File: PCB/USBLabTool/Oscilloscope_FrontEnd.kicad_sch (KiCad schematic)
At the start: 92 parts, among them J10 T_pwm, J11 T_buf, J12 T_buf, J13 ADC2, J14 ADC1, J15 +3.3VA, J16 +3.3VA, J3 T_att, J4 T_att, J5 T_acdc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

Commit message: final version prototype
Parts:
- D1: footprint Diode_THT:D_DO-35_SOD27_P7.62mm_Horizontal -> Diode_SMD:D_SOD-323_HandSoldering
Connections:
- net GND: no longer C1.1, C4.2, C5.1, C8.2, R2.1, R3.1, R5.1, R8.1
- net GNDA: now also C1.1, C4.2, C5.1, C8.2, R2.1, R3.1, R5.1, R8.1

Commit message: change scope diode footprint
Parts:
- D2: footprint Diode_THT:D_DO-35_SOD27_P7.62mm_Horizontal -> Diode_SMD:D_SOD-323_HandSoldering
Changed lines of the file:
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@@
 			)
 		)
-		(property "Footprint" "Diode_THT:D_DO-35_SOD27_P7.62mm_Horizontal"
+		(property "Footprint" "Diode_SMD:D_SOD-323_HandSoldering"
 			(at 69.85 60.325 0)
 			(effects
@@
 			(at 69.85 55.88 0)
 			(effects
+				(font
+					(size 1.27 1.27)
+				)
+				(hide yes)
+			)
+		)
+		(property "Purpose" ""
+			(at 69.85 55.88 0)
+			(effects

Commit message: PCB updates from meeting 3/19
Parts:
- removed J3, J4: T_att, Connector_PinHeader_2.54mm:PinHeader_1x01_P2.54mm_Vertical, symbol Connector_Generic:Conn_01x01
- removed J5, J6: T_acdc, Connector_PinHeader_2.54mm:PinHeader_1x01_P2.54mm_Vertical, symbol Connector_Generic:Conn_01x01
- J10, J11, J12, J13, J14, J15, J16, J7, J9: footprint Connector_PinHeader_2.54mm:PinHeader_1x01_P2.54mm_Vertical -> TestPoint:TestPoint_Pad_D2.0mm

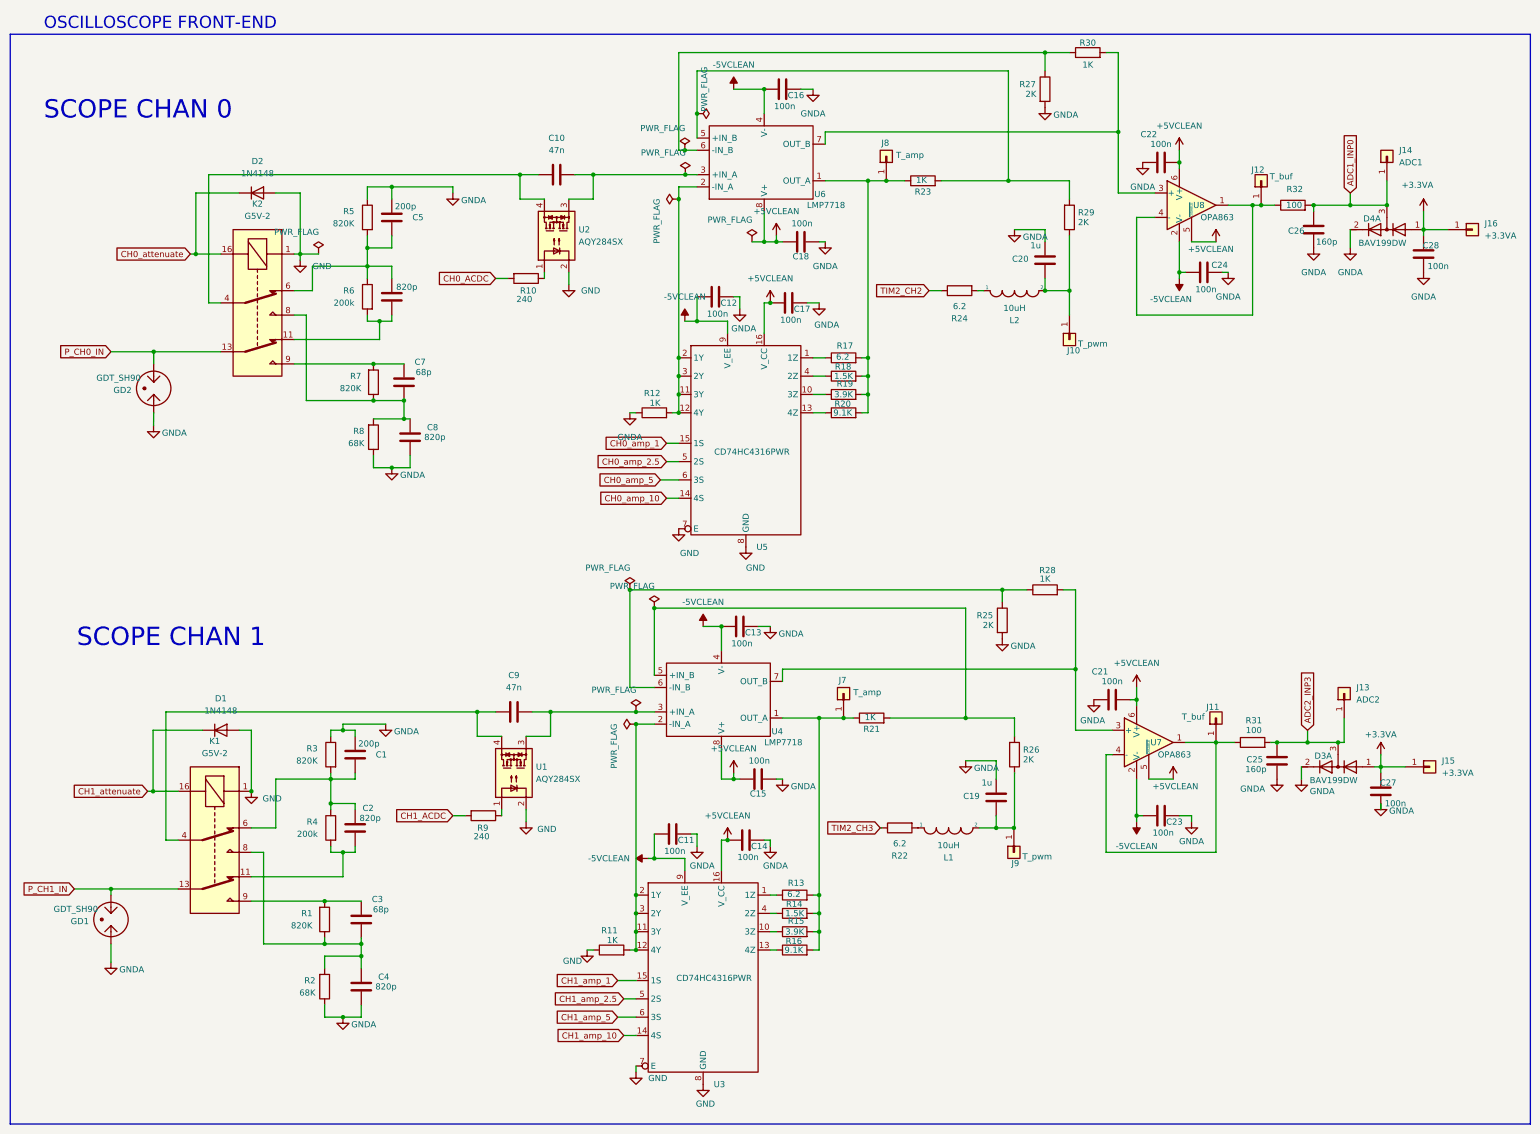
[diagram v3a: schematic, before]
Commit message: Resolved DRC/ERC errors in PCB and schematic
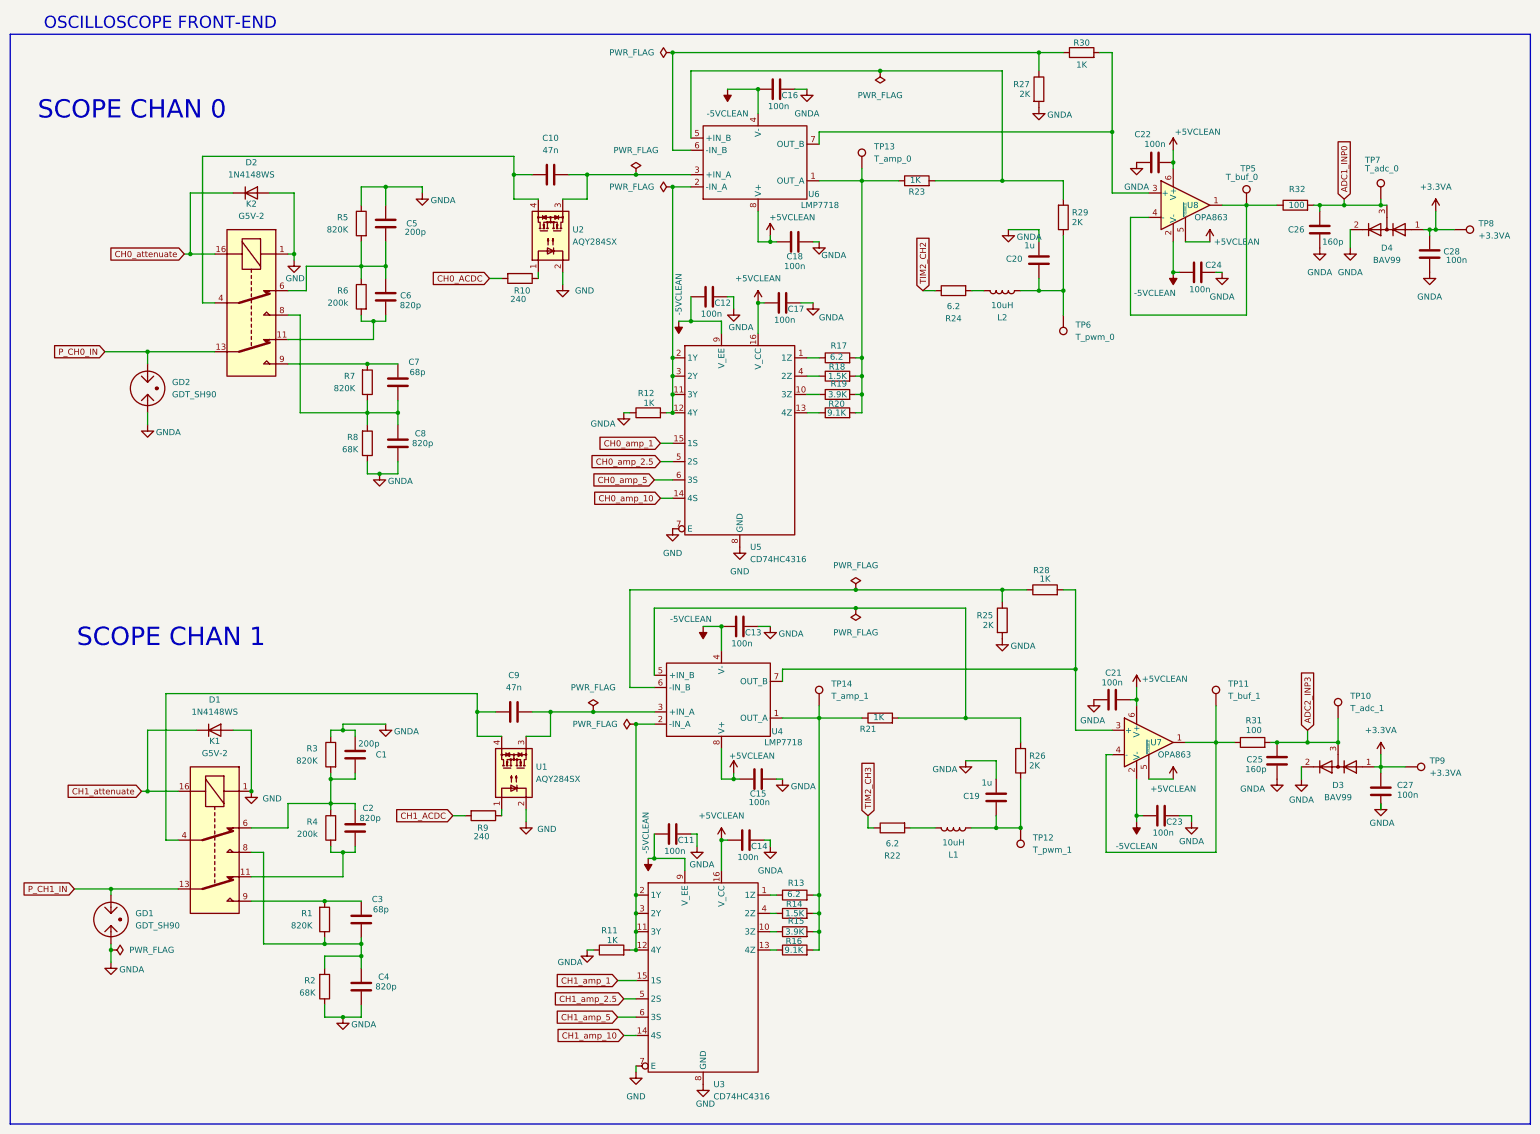
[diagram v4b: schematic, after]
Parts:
- removed D1, D2: 1N4148, Diode_SMD:D_SOD-323_HandSoldering, symbol Diode:1N4148
- removed D3, D4: BAV199DW, Package_TO_SOT_SMD:SOT-363_SC-70-6_Handsoldering, symbol Diode:BAV199DW
- removed GD1, GD2: GDT_SH90, userfp:GDT_SH_LTF, symbol Device:GDT_2Pin
- removed J10, J9: T_pwm, TestPoint:TestPoint_Pad_D2.0mm, symbol Connector_Generic:Conn_01x01
- removed J11, J12: T_buf, TestPoint:TestPoint_Pad_D2.0mm, symbol Connector_Generic:Conn_01x01
- removed J13: ADC2, TestPoint:TestPoint_Pad_D2.0mm, symbol Connector_Generic:Conn_01x01
- removed J14: ADC1, TestPoint:TestPoint_Pad_D2.0mm, symbol Connector_Generic:Conn_01x01
- removed J15, J16: +3.3VA, TestPoint:TestPoint_Pad_D2.0mm, symbol Connector_Generic:Conn_01x01
- removed J7: T_amp, TestPoint:TestPoint_Pad_D2.0mm, symbol Connector_Generic:Conn_01x01
- removed J8: T_amp, Connector_PinHeader_2.54mm:PinHeader_1x01_P2.54mm_Vertical, symbol Connector_Generic:Conn_01x01
- removed L1, L2: 10uH, Inductor_SMD:L_0603_1608Metric_Pad1.05x0.95mm_HandSolder, symbol pspice:INDUCTOR
- removed U3, U5: CD74HC4316PWR, Package_SO:TSSOP-16_4.4x5mm_P0.65mm, symbol USBLabTool:CD74HC4316M96
- added D1, D2: 1N4148WS, Diode_SMD:D_SOD-323, symbol Diode:1N4148WS
- added D3, D4: BAV99, Package_TO_SOT_SMD:SOT-23, symbol Diode:BAV99
- added GD1, GD2: GDT_SH90, userfp:GDT_SH_LTF, symbol USBLabTool:GDT_2Pin
- added L1, L2: 10uH, Inductor_SMD:L_0603_1608Metric_Pad1.05x0.95mm_HandSolder, symbol Device:L
- added TP10: T_adc_1, TestPoint:TestPoint_Pad_D2.0mm, symbol Connector:TestPoint
- added TP11: T_buf_1, TestPoint:TestPoint_Pad_D2.0mm, symbol Connector:TestPoint
- added TP12: T_pwm_1, TestPoint:TestPoint_Pad_D2.0mm, symbol Connector:TestPoint
- added TP13: T_amp_0, TestPoint:TestPoint_Pad_D2.0mm, symbol Connector:TestPoint
- added TP14: T_amp_1, TestPoint:TestPoint_Pad_D2.0mm, symbol Connector:TestPoint
- added TP5: T_buf_0, TestPoint:TestPoint_Pad_D2.0mm, symbol Connector:TestPoint
- added TP6: T_pwm_0, TestPoint:TestPoint_Pad_D2.0mm, symbol Connector:TestPoint
- added TP7: T_adc_0, TestPoint:TestPoint_Pad_D2.0mm, symbol Connector:TestPoint
- added TP8, TP9: +3.3VA, TestPoint:TestPoint_Pad_D2.0mm, symbol Connector:TestPoint
- added U3, U5: CD74HC4316, Package_SO:TSSOP-16_4.4x5mm_P0.65mm, symbol USBLabTool:CD74HC4316
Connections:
- net +3.3VA: now also D3.1 (K), D4.1 (K), TP8.1, TP9.1
- net +5VCLEAN: now also U3.16 (V_CC), U5.16 (V_CC)
- net -5VCLEAN: now also U3.9 (V_EE), U5.9 (V_EE)
- net ADC1_INP0: now also D4.3 (K), TP7.1
- net ADC2_INP3: now also D3.3 (K), TP10.1
- net CH0_amp_1: now also U5.15 (1S)
- net CH0_amp_10: now also U5.14 (4S)
- net CH0_amp_2.5: now also U5.5 (2S)
- net CH0_amp_5: now also U5.6 (3S)
- net CH0_attenuate: now also D2.1 (K)
- net CH1_amp_1: now also U3.15 (1S)
- net CH1_amp_10: now also U3.14 (4S)
- net CH1_amp_2.5: now also U3.5 (2S)
- net CH1_amp_5: now also U3.6 (3S)
- net CH1_attenuate: now also D1.1 (K)
- net GND: now also D1.2 (A), D2.2 (A), U3.7 (E), U3.8 (GND), U5.7 (E), U5.8 (GND); no longer R11.1
- net GNDA: now also R11.1, D3.2 (A), D4.2 (A), GD1.1, GD2.1
- net P_CH0_IN: now also GD2.2
- net P_CH1_IN: now also GD1.2
- net at R17.2, R18.2, R19.2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: now also TP13.1
- net at R13.1: now also U3.1 (1Z)
- net at R13.2, R14.2, R15.2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: now also TP14.1
- net at R17.1: now also U5.1 (1Z)
- net at R15.1: now also U3.10 (3Z)
- net at R20.1: now also U5.13 (4Z)
- net at R32.1, U8.1, U8.4 (-): now also TP5.1
- net at C20.1, R29.1: now also L2.2, TP6.1
- net at R31.1, U7.1, U7.4 (-): now also TP11.1
- net at C19.1, R26.1: now also L1.2, TP12.1
- net at R14.1: now also U3.4 (2Z)
- net at R12.2, U6.2 (-IN_A): now also U5.11 (3Y), U5.12 (4Y), U5.2 (1Y), U5.3 (2Y)
- net at R11.2, U4.2 (-IN_A): now also U3.11 (3Y), U3.12 (4Y), U3.2 (1Y), U3.3 (2Y)
- net at R19.1: now also U5.10 (3Z)
- net at R24.2: now also L2.1
- net at R18.1: now also U5.4 (2Z)
- net at R16.1: now also U3.13 (4Z)
- net at R22.2: now also L1.1
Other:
- moved on the sheet: C10, C12, C16, C17, C18, C20, C22, C24, C26, C28, C5, C7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
